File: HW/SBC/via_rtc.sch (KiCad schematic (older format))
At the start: 11 parts, among them J1 VIA1PA, J2 VIA1PB, J3 VIA2PB, U4 DS1511Y+, U5 WD65C22PLCC44, U6 WD65C22PLCC44

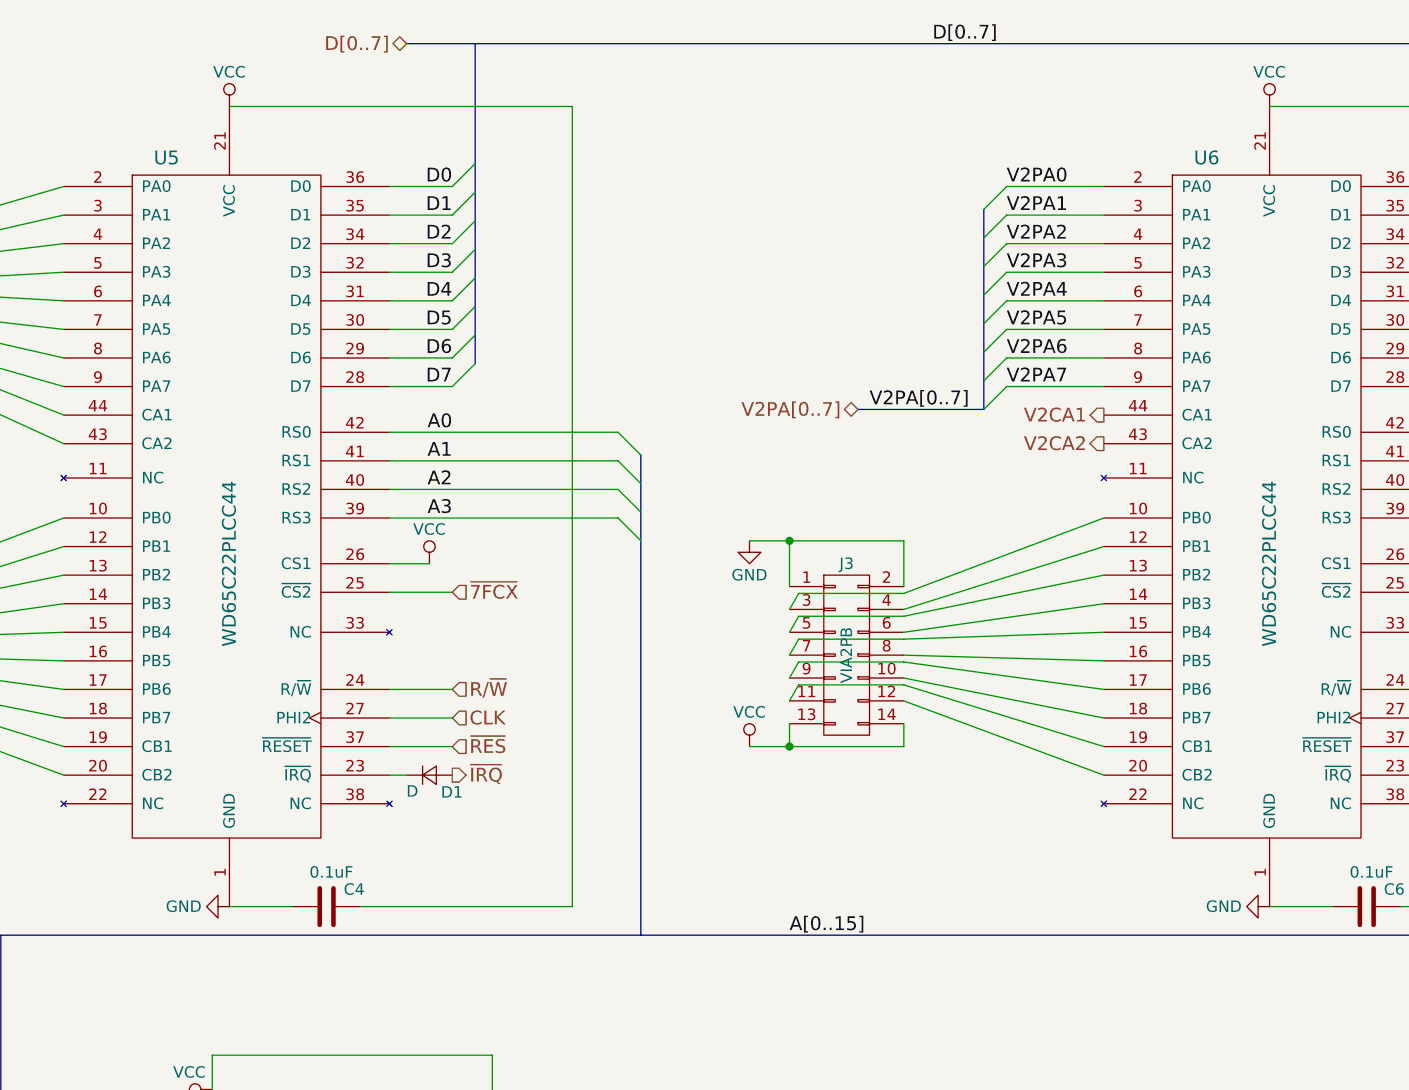
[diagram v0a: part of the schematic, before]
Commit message: Added CPLD to schematics. Updates rest of schematics to use CPLD
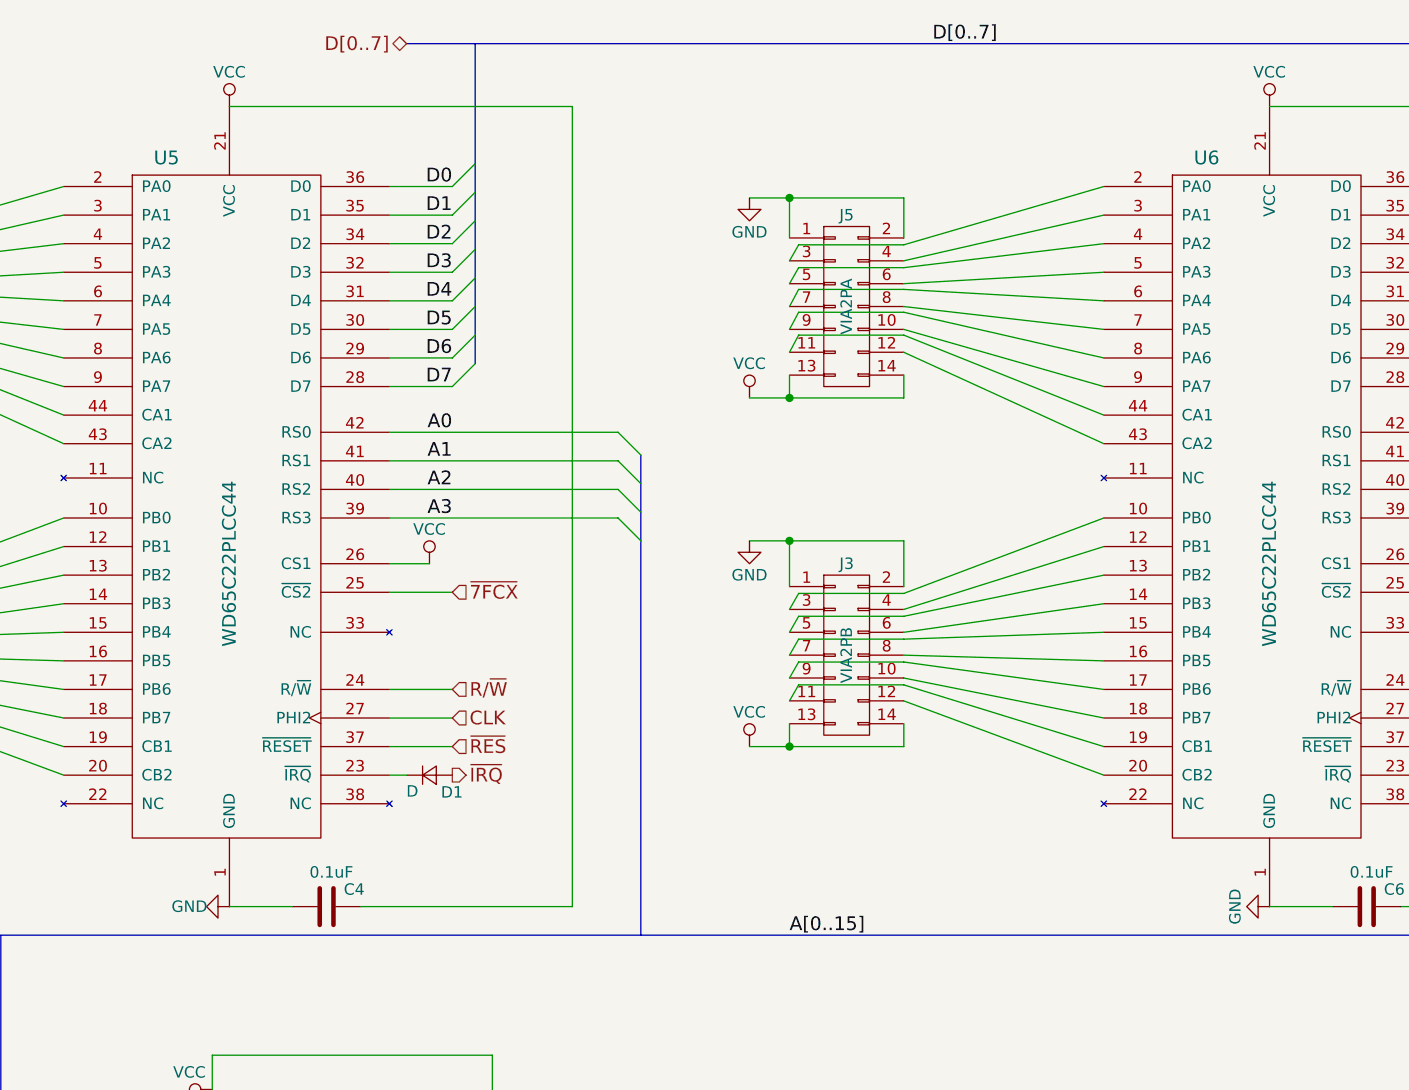
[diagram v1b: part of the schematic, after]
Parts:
- added J5: VIA2PA, Connectors_IDC:IDC-Header_2x07_Pitch2.54mm_Straight, symbol CONN_02X07
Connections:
- net GND: now also J5.1 (P1), J5.2 (P2)
- net VCC: now also J5.13 (P13), J5.14 (P14)
- net V2CA1: no longer names the net of U6.44 (CA1)
- net V2CA1: now also J5.11 (P11)
- net V2CA2: no longer names the net of U6.43 (CA2)
- net V2CA2: now also J5.12 (P12)
- net V2PA0: no longer names the net of U6.2 (PA0)
- net V2PA0: now also J5.3 (P3)
- net V2PA1: no longer names the net of U6.3 (PA1)
- net V2PA1: now also J5.4 (P4)
- net V2PA2: no longer names the net of U6.4 (PA2)
- net V2PA2: now also J5.5 (P5)
- net V2PA3: no longer names the net of U6.5 (PA3)
- net V2PA3: now also J5.6 (P6)
- net V2PA4: no longer names the net of U6.6 (PA4)
- net V2PA4: now also J5.7 (P7)
- net V2PA5: no longer names the net of U6.7 (PA5)
- net V2PA5: now also J5.8 (P8)
- net V2PA6: no longer names the net of U6.8 (PA6)
- net V2PA6: now also J5.9 (P9)
- net V2PA7: no longer names the net of U6.9 (PA7)
- net V2PA7: now also J5.10 (P10)
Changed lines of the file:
@@
 $Descr A4 11693 8268
 encoding utf-8
-Sheet 3 8
+Sheet 3 7
 Title "VIA and RTC"
 Date "2017-03-25"
@@
 $EndComp
 $Comp
-L GND #PWR08
-U 1 1 58D6939F
-P 700 2825
-F 0 "#PWR08" H 700 2575 50  0001 C CNN
-F 1 "GND" H 700 2675 50  0000 C CNN
-F 2 "" H 700 2825 50  0001 C CNN
-F 3 "" H 700 2825 50  0001 C CNN
-	1    700  2825
-	1    0    0    -1
-$EndComp
-$Comp
-L GND #PWR09
-U 1 1 58D6973D
-P 700 1325
-F 0 "#PWR09" H 700 1075 50  0001 C CNN
-F 1 "GND" H 700 1175 50  0000 C CNN
-F 2 "" H 700 1325 50  0001 C CNN
-F 3 "" H 700 1325 50  0001 C CNN
-	1    700  1325
-	1    0    0    -1
-$EndComp
-$Comp
-L VCC #PWR010
+L VCC #PWR08
 U 1 1 58D69759
 P 700 2200
-F 0 "#PWR010" H 700 2050 50  0001 C CNN
+F 0 "#PWR08" H 700 2050 50  0001 C CNN
 F 1 "VCC" H 700 2350 50  0000 C CNN
 F 2 "" H 700 2200 50  0001 C CNN
 F 3 "" H 700 2200 50  0001 C CNN
 	1    700  2200
-	1    0    0    -1
-$EndComp
-$Comp
-L VCC #PWR011
-U 1 1 58D6982A
-P 3850 2925
-F 0 "#PWR011" H 3850 2775 50  0001 C CNN
-F 1 "VCC" H 3850 3075 50  0000 C CNN
-F 2 "" H 3850 2925 50  0001 C CNN
-F 3 "" H 3850 2925 50  0001 C CNN
-	1    3850 2925
 	1    0    0    -1
 $EndComp
@@
 $EndComp
 $Comp
-L VCC #PWR012
-U 1 1 5924C298
-P 2975 925
-F 0 "#PWR012" H 2975 775 50  0001 C CNN
-F 1 "VCC" H 2975 1075 50  0000 C CNN
-F 2 "" H 2975 925 50  0001 C CNN
-F 3 "" H 2975 925 50  0001 C CNN
-	1    2975 925
-	1    0    0    -1
-$EndComp
-$Comp
-L GND #PWR013
-U 1 1 5924C3BB
-P 2975 4425
-F 0 "#PWR013" H 2975 4175 50  0001 C CNN
-F 1 "GND" V 2975 4225 50  0000 C CNN
-F 2 "" H 2975 4425 50  0001 C CNN
-F 3 "" H 2975 4425 50  0001 C CNN
-	1    2975 4425
-	0    1    1    0
-$EndComp
-$Comp
-L VCC #PWR014
+L VCC #PWR09
 U 1 1 5924C55A
 P 2900 5225
-F 0 "#PWR014" H 2900 5075 50  0001 C CNN
+F 0 "#PWR09" H 2900 5075 50  0001 C CNN
 F 1 "VCC" V 2975 5325 50  0000 C CNN
 F 2 "" H 2900 5225 50  0001 C CNN
@@
 	1    2900 5225
 	0    -1   -1   0
-$EndComp
-$Comp
-L GND #PWR015
-U 1 1 5924C775
-P 2825 7100
-F 0 "#PWR015" H 2825 6850 50  0001 C CNN
-F 1 "GND" H 2825 6950 50  0000 C CNN
-F 2 "" H 2825 7100 50  0001 C CNN
-F 3 "" H 2825 7100 50  0001 C CNN
-	1    2825 7100
-	1    0    0    -1
 $EndComp
 $Comp
@@
 $EndComp
 $Comp
-L VCC #PWR016
+L VCC #PWR010
 U 1 1 5930635F
 P 5250 3725
-F 0 "#PWR016" H 5250 3575 50  0001 C CNN
+F 0 "#PWR010" H 5250 3575 50  0001 C CNN
 F 1 "VCC" H 5250 3875 50  0000 C CNN
 F 2 "" H 5250 3725 50  0001 C CNN
@@
 $EndComp
 $Comp
-L GND #PWR017
+L GND #PWR011
 U 1 1 59306365
 P 5250 2825
-F 0 "#PWR017" H 5250 2575 50  0001 C CNN
+F 0 "#PWR011" H 5250 2575 50  0001 C CNN
 F 1 "GND" H 5250 2675 50  0000 C CNN
 F 2 "" H 5250 2825 50  0001 C CNN
@@
 $EndComp
 $Comp
-L VCC #PWR018
+L VCC #PWR012
 U 1 1 59306377
 P 8400 2925
-F 0 "#PWR018" H 8400 2775 50  0001 C CNN
+F 0 "#PWR012" H 8400 2775 50  0001 C CNN
 F 1 "VCC" H 8400 3075 50  0000 C CNN
 F 2 "" H 8400 2925 50  0001 C CNN
@@
 	0    1    1    0
 $EndComp
-$Comp
-L VCC #PWR019
-U 1 1 593063DC
-P 7525 925
-F 0 "#PWR019" H 7525 775 50  0001 C CNN
-F 1 "VCC" H 7525 1075 50  0000 C CNN
-F 2 "" H 7525 925 50  0001 C CNN
-F 3 "" H 7525 925 50  0001 C CNN
-	1    7525 925
-	1    0    0    -1
-$EndComp
-$Comp
-L GND #PWR020
-U 1 1 593063E2
-P 7525 4425
-F 0 "#PWR020" H 7525 4175 50  0001 C CNN
-F 1 "GND" V 7525 4225 50  0000 C CNN
-F 2 "" H 7525 4425 50  0001 C CNN
-F 3 "" H 7525 4425 50  0001 C CNN
-	1    7525 4425
-	0    1    1    0
-$EndComp
-Text Label 6375 1275 0    60   ~ 0
-V2PA0
-Text Label 6375 1400 0    60   ~ 0
-V2PA1
-Text Label 6375 1525 0    60   ~ 0
-V2PA2
-Text Label 6375 1650 0    60   ~ 0
-V2PA3
-Text Label 6375 1775 0    60   ~ 0
-V2PA4
-Text Label 6375 1900 0    60   ~ 0
-V2PA5
-Text Label 6375 2025 0    60   ~ 0
-V2PA6
-Text Label 6375 2150 0    60   ~ 0
-V2PA7
-Entry Wire Line
-	6275 1375 6375 1275
-Entry Wire Line
-	6275 1500 6375 1400
-Entry Wire Line
-	6275 1625 6375 1525
-Entry Wire Line
-	6275 1750 6375 1650
-Entry Wire Line
-	6275 1875 6375 1775
-Entry Wire Line
-	6275 2000 6375 1900
-Entry Wire Line
-	6275 2125 6375 2025
-Entry Wire Line
-	6275 2250 6375 2150
-Text Label 5775 2250 0    60   ~ 0
-V2PA[0..7]
-Text HLabel 5725 2250 0    60   BiDi ~ 0
-V2PA[0..7]
 Text Label 8500 1275 2    60   ~ 0
 D0
@@
 Text HLabel 3950 3850 2    60   Output ~ 0
 ~IRQ
-Text HLabel 6800 2275 0    60   Output ~ 0
-V2CA1
-Text HLabel 6800 2400 0    60   Output ~ 0
-V2CA2
 Wire Wire Line
 	2400 5925 2075 5925
@@
 Wire Wire Line
 	9025 925  7525 925
-Wire Wire Line
-	6800 1275 6375 1275
-Wire Wire Line
-	6800 1400 6375 1400
-Wire Wire Line
-	6800 1525 6375 1525
-Wire Wire Line
-	6800 1650 6375 1650
-Wire Wire Line
-	6800 1775 6375 1775
-Wire Wire Line
-	6800 1900 6375 1900
-Wire Wire Line
-	6800 2025 6375 2025
-Wire Wire Line
-	6800 2150 6375 2150
-Wire Bus Line
-	6275 1375 6275 2250
-Wire Bus Line
-	6275 2250 5725 2250
 Wire Wire Line
 	3675 1275 3950 1275
@@
 	1    0    0    -1
 $EndComp
+$Comp
+L CONN_02X07 J5
+U 1 1 5A14CA2C
+P 5675 1800
+F 0 "J5" H 5675 2200 50  0000 C CNN
+F 1 "VIA2PA" V 5675 1800 50  0000 C CNN
+F 2 "Connectors_IDC:IDC-Header_2x07_Pitch2.54mm_Straight" H 5675 600 50  0001 C CNN
+F 3 "" H 5675 600 50  0001 C CNN
+	1    5675 1800
+	1    0    0    -1
+$EndComp
+$Comp
+L GND #PWR013
+U 1 1 5A14CA32
+P 5250 1325
+F 0 "#PWR013" H 5250 1075 50  0001 C CNN
+F 1 "GND" H 5250 1175 50  0000 C CNN
+F 2 "" H 5250 1325 50  0001 C CNN
+F 3 "" H 5250 1325 50  0001 C CNN
+	1    5250 1325
+	1    0    0    -1
+$EndComp
+$Comp
+L VCC #PWR014
+U 1 1 5A14CA38
+P 5250 2200
+F 0 "#PWR014" H 5250 2050 50  0001 C CNN
+F 1 "VCC" H 5250 2350 50  0000 C CNN
+F 2 "" H 5250 2200 50  0001 C CNN
+F 3 "" H 5250 2200 50  0001 C CNN
+	1    5250 2200
+	1    0    0    -1
+$EndComp
+Wire Wire Line
+	6800 1275 5925 1530
+Wire Wire Line
+	5925 1530 5465 1530
+Wire Wire Line
+	5465 1530 5425 1600
+Wire Wire Line
+	6800 1525 5925 1630
+Wire Wire Line
+	5925 1630 5465 1630
+Wire Wire Line
+	5465 1630 5425 1700
+Wire Wire Line
+	5425 1800 5465 1725
+Wire Wire Line
+	5425 1900 5465 1825
+Wire Wire Line
+	5425 2000 5465 1925
+Wire Wire Line
+	6800 1775 5925 1725
+Wire Wire Line
+	5925 1725 5465 1725
+Wire Wire Line
+	5465 1825 5925 1825
+Wire Wire Line
+	5465 1925 5925 1925
+Wire Wire Line
+	5925 1825 6800 2025
+Wire Wire Line
+	5925 1925 6800 2275
+Wire Wire Line
+	6800 1400 5925 1600
+Wire Wire Line
+	6800 1650 5925 1700
+Wire Wire Line
+	6800 1900 5925 1800
+Wire Wire Line
+	6800 2150 5925 1900
+Wire Wire Line
+	6800 2400 5925 2000
+Wire Wire Line
+	5925 2200 5925 2100
+Wire Wire Line
+	5250 2200 5925 2200
+Wire Wire Line
+	5425 2200 5425 2100
+Connection ~ 5425 2200
+Wire Wire Line
+	5925 1325 5925 1500
+Wire Wire Line
+	5250 1325 5925 1325
+Wire Wire Line
+	5425 1325 5425 1500
+Connection ~ 5425 1325
+$Comp
+L VCC #PWR015
+U 1 1 5A161450
+P 3850 2925
+F 0 "#PWR015" H 3850 2775 50  0001 C CNN
+F 1 "VCC" H 3850 3075 50  0000 C CNN
+F 2 "" H 3850 2925 50  0001 C CNN
+F 3 "" H 3850 2925 50  0001 C CNN
+	1    3850 2925
+	1    0    0    -1
+$EndComp
+$Comp
+L VCC #PWR016
+U 1 1 5A16185F
+P 2975 925
+F 0 "#PWR016" H 2975 775 50  0001 C CNN
+F 1 "VCC" H 2975 1075 50  0000 C CNN
+F 2 "" H 2975 925 50  0001 C CNN
+F 3 "" H 2975 925 50  0001 C CNN
+	1    2975 925
+	1    0    0    -1
+$EndComp
+$Comp
+L GND #PWR017
+U 1 1 5A161FC3
+P 700 1325
+F 0 "#PWR017" H 700 1075 50  0001 C CNN
+F 1 "GND" H 700 1175 50  0000 C CNN
+F 2 "" H 700 1325 50  0001 C CNN
+F 3 "" H 700 1325 50  0001 C CNN
+	1    700  1325
+	1    0    0    -1
+$EndComp
+$Comp
+L GND #PWR018
+U 1 1 5A16238A
+P 7525 4425
+F 0 "#PWR018" H 7525 4175 50  0001 C CNN
+F 1 "GND" H 7525 4275 50  0000 C CNN
+F 2 "" H 7525 4425 50  0001 C CNN
+F 3 "" H 7525 4425 50  0001 C CNN
+	1    7525 4425
+	0    1    1    0
+$EndComp
+$Comp
+L GND #PWR019
+U 1 1 5A162751
+P 2825 7100
+F 0 "#PWR019" H 2825 6850 50  0001 C CNN
+F 1 "GND" H 2825 6950 50  0000 C CNN
+F 2 "" H 2825 7100 50  0001 C CNN
+F 3 "" H 2825 7100 50  0001 C CNN
+	1    2825 7100
+	1    0    0    -1
+$EndComp
+$Comp
+L GND #PWR020
+U 1 1 5A162B3C
+P 700 2825
+F 0 "#PWR020" H 700 2575 50  0001 C CNN
+F 1 "GND" H 700 2675 50  0000 C CNN
+F 2 "" H 700 2825 50  0001 C CNN
+F 3 "" H 700 2825 50  0001 C CNN
+	1    700  2825
+	1    0    0    -1
+$EndComp
+$Comp
+L VCC #PWR021
+U 1 1 5A1631AF
+P 7525 925
+F 0 "#PWR021" H 7525 775 50  0001 C CNN
+F 1 "VCC" H 7525 1075 50  0000 C CNN
+F 2 "" H 7525 925 50  0001 C CNN
+F 3 "" H 7525 925 50  0001 C CNN
+	1    7525 925
+	1    0    0    -1
+$EndComp
+$Comp
+L GND #PWR022
+U 1 1 5A16371D
+P 2975 4425
+F 0 "#PWR022" H 2975 4175 50  0001 C CNN
+F 1 "GND" V 2975 4250 50  0000 C CNN
+F 2 "" H 2975 4425 50  0001 C CNN
+F 3 "" H 2975 4425 50  0001 C CNN
+	1    2975 4425
+	0    1    1    0
+$EndComp
 $EndSCHEMATC
